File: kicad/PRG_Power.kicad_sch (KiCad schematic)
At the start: 18 parts, among them U1 4049

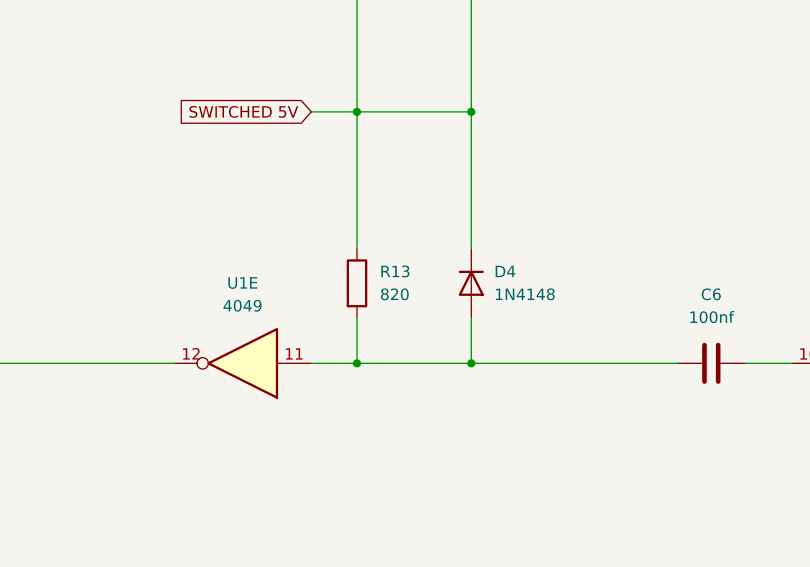
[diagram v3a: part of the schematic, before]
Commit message: Minor error - wrong resistor value as R13
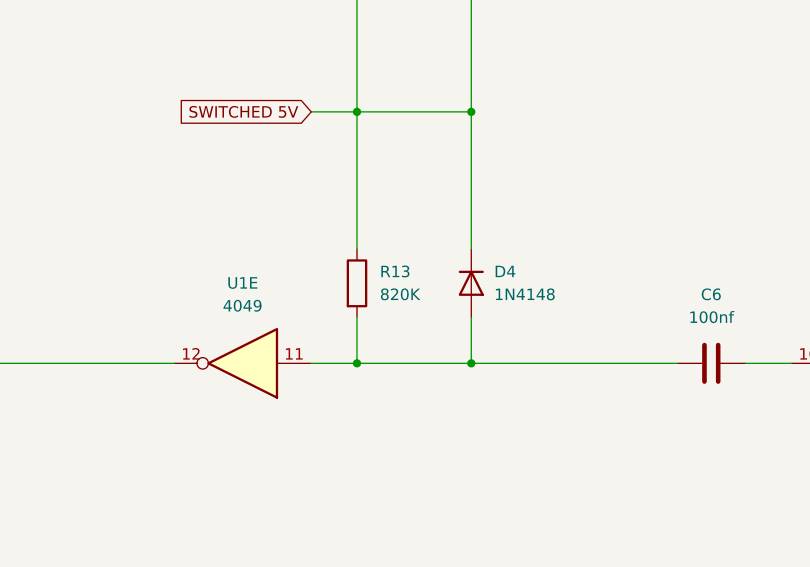
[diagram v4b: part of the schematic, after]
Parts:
- R13: value 820 -> 820K
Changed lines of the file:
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@@
   (title_block
     (title "EPROM Burner 2708 / 2716")
-    (date "2023-08-14")
-    (rev "2.5")
+    (date "2023-09-01")
+    (rev "2.6")
   )
   (junction (at 180.34 101.6) (diameter 0) (color 0 0 0 0)
@@
   (symbol (lib_id "Device:R") (at 180.34 92.71 0) (unit 1)
     (in_bom yes) (on_board yes) (dnp no) (fields_autoplaced)
-    (property "Reference" "R13" (at 182.88 91.4399 0)
-      (effects (font (size 1.27 1.27)) (justify left))
-    )
-    (property "Value" "820" (at 182.88 93.9799 0)
-      (effects (font (size 1.27 1.27)) (justify left))
-    )
+    (property "Reference" "R13" (at 182.88 91.44 0)
+      (effects (font (size 1.27 1.27)) (justify left))
+    )
+    (property "Value" "820K" (at 182.88 93.98 0)
+      (effects (font (size 1.27 1.27)) (justify left))
+    )

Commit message: Update docs
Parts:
- TR3, TR4, TR5: footprint Package_TO_SOT_THT:TO-92_Inline_Wide -> Package_TO_SOT_THT:TO-92_Inline
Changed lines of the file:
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@@
 (kicad_sch
-	(version 20231120)
+	(version 20250114)
 	(generator "eeschema")
-	(generator_version "8.0")
+	(generator_version "9.0")
 	(paper "A4")
 	(title_block
 		(title "EPROM Burner 2708 / 2716")
-		(date "2023-09-01")
-		(rev "2.6")
+		(date "2025-04-14")
+		(rev "2.7")
 	)
 	(junction
@@
 			)
 		)
-		(property "Footprint" "Package_TO_SOT_THT:TO-92_Inline_Wide"
+		(property "Footprint" "Package_TO_SOT_THT:TO-92_Inline"
 			(at 99.06 62.865 0)
 			(effects
@@
 			)
 		)
-		(property "Description" ""
+		(property "Description" "0.1A Ic, 30V Vce, PNP Small Signal Transistor, TO-92"
 			(at 104.14 60.96 0)
 			(effects
@@
 			)
 		)
-		(property "Description" ""
+		(property "Description" "Power symbol creates a global label with name \"GND\" , ground"
 			(at 116.84 38.1 0)
 			(effects
@@
 			)
 		)
-		(property "Description" ""
+		(property "Description" "Resistor"
 			(at 180.34 92.71 0)
 			(effects
@@
 			)
 		)
-		(property "Description" ""
+		(property "Description" "100V 0.15A standard switching diode, DO-35"
+			(at 193.04 92.71 0)
+			(effects
+				(font
+					(size 1.27 1.27)
+				)
+				(hide yes)
+			)
+		)
+		(property "Sim.Device" "D"
+			(at 193.04 92.71 0)
+			(effects
+				(font
+					(size 1.27 1.27)
+				)
+				(hide yes)
+			)
+		)
+		(property "Sim.Pins" "1=K 2=A"
 			(at 193.04 92.71 0)
 			(effects
@@
 			)
 		)
-		(property "Footprint" "Package_TO_SOT_THT:TO-92_Inline_Wide"
+		(property "Footprint" "Package_TO_SOT_THT:TO-92_Inline"
 			(at 121.92 46.355 0)
 			(effects
@@
 			)
 		)
-		(property "Description" ""
+		(property "Description" "0.1A Ic, 30V Vce, Small Signal NPN Transistor, TO-92"
 			(at 127 48.26 0)
 			(effects
@@
 			)
 		)
-		(property "Description" ""
+		(property "Description" "Unpolarized capacitor"
 			(at 219.71 101.6 0)
 			(effects
@@
 			)
 		)
-		(property "Description" ""
+		(property "Description" "Resistor"
 			(at 115.57 30.48 0)
 			(effects
@@
 			)
 		)
-		(property "Description" ""
+		(property "Description" "Power symbol creates a global label with name \"GND\" , ground"
 			(at 261.62 116.84 0)
 			(effects
@@
 			)
 		)
-		(property "Description" ""
+		(property "Description" "Power symbol creates a global label with name \"GND\" , ground"
 			(at 86.36 25.4 0)
 			(effects
@@
 			)
 		)
-		(property "Description" ""
+		(property "Description" "Resistor"
 			(at 109.22 69.85 0)
 			(effects
@@
 			)
 		)
-		(property "Description" ""
+		(property "Description" "Unpolarized capacitor"
 			(at 60.96 59.69 0)
 			(effects
@@
 			)
 		)
-		(property "Description" ""
+		(property "Description" "Resistor"
 			(at 101.6 41.91 0)
 			(effects
@@
 			)
 		)
-		(property "Description" ""
+		(property "Description" "Resistor"
 			(at 261.62 110.49 0)
 			(effects
@@
 			)
 		)
-		(property "Description" ""
+		(property "Description" "Hex Buffer Inverter"
 			(at 149.86 40.64 0)
 			(effects
@@
 			)
 		)
-		(property "Description" ""
+		(property "Description" "Resistor"
 			(at 115.57 60.96 0)
 			(effects
@@
 			)
 		)
-		(property "Description" ""
+		(property "Description" "Unpolarized capacitor"
 			(at 217.17 48.26 0)
 			(effects
@@
 			)
 		)
-		(property "Footprint" "Package_TO_SOT_THT:TO-92_Inline_Wide"
+		(property "Footprint" "Package_TO_SOT_THT:TO-92_Inline"
 			(at 99.06 28.575 0)
 			(effects
@@
 			)
 		)
-		(property "Description" ""
+		(property "Description" "0.1A Ic, 30V Vce, Small Signal NPN Transistor, TO-92"
 			(at 104.14 30.48 0)
 			(effects
@@
 			)
 		)
-		(property "Description" ""
+		(property "Description" "Hex Buffer Inverter"
 			(at 167.64 101.6 0)
 			(effects
@@
 			)
 		)
-		(property "Description" ""
+		(property "Description" "Resistor"
 			(at 140.97 48.26 0)
 			(effects
@@
 			)
 		)
-		(property "Description" ""
+		(property "Description" "Power symbol creates a global label with name \"GND\" , ground"
 			(at 60.96 63.5 0)
 			(effects
@@
 			)
 		)
-		(property "Description" ""
+		(property "Description" "Hex Buffer Inverter"
 			(at 236.22 101.6 0)
 			(effects
@@
 			)
 		)
-		(property "Description" ""
+		(property "Description" "Resistor"
 			(at 180.34 57.15 0)
 			(effects
@@
 			)
 		)
-		(property "Description" ""
+		(property "Description" "100V 0.15A standard switching diode, DO-35"
+			(at 193.04 57.15 0)
+			(effects
+				(font
+					(size 1.27 1.27)
+				)
+				(hide yes)
+			)
+		)
+		(property "Sim.Device" "D"
+			(at 193.04 57.15 0)
+			(effects
+				(font
+					(size 1.27 1.27)
+				)
+				(hide yes)
+			)
+		)
+		(property "Sim.Pins" "1=K 2=A"
 			(at 193.04 57.15 0)
 			(effects
@@
 			)
 		)
-		(property "Description" ""
+		(property "Description" "Hex Buffer Inverter"
 			(at 167.64 48.26 0)
 			(effects
@@
 			)
 		)
-		(property "Description" ""
+		(property "Description" "Resistor"
 			(at 80.01 50.8 0)
 			(effects
@@
 			)
 		)
-		(property "Description" ""
+		(property "Description" "Hex Buffer Inverter"
 			(at 233.68 48.26 0)
 			(effects

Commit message: Update footprints
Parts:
- D3, D4: footprint Diode_THT:D_DO-35_SOD27_P7.62mm_Horizontal -> Diode_THT:D_DO-41_SOD81_P10.16mm_Horizontal
- TR3, TR4, TR5: footprint Package_TO_SOT_THT:TO-92_Inline -> Package_TO_SOT_THT:TO-92_Inline_Wide
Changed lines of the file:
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@@
 			)
 		)
-		(property "Footprint" "Package_TO_SOT_THT:TO-92_Inline"
+		(property "Footprint" "Package_TO_SOT_THT:TO-92_Inline_Wide"
 			(at 99.06 62.865 0)
 			(effects
@@
 			)
 		)
-		(property "Footprint" "Diode_THT:D_DO-35_SOD27_P7.62mm_Horizontal"
+		(property "Footprint" "Diode_THT:D_DO-41_SOD81_P10.16mm_Horizontal"
 			(at 188.595 92.71 0)
 			(effects
@@
 			)
 		)
-		(property "Footprint" "Package_TO_SOT_THT:TO-92_Inline"
+		(property "Footprint" "Package_TO_SOT_THT:TO-92_Inline_Wide"
 			(at 121.92 46.355 0)
 			(effects
@@
 			)
 		)
-		(property "Footprint" "Package_TO_SOT_THT:TO-92_Inline"
+		(property "Footprint" "Package_TO_SOT_THT:TO-92_Inline_Wide"
 			(at 99.06 28.575 0)
 			(effects
@@
 			)
 		)
-		(property "Footprint" "Diode_THT:D_DO-35_SOD27_P7.62mm_Horizontal"
+		(property "Footprint" "Diode_THT:D_DO-41_SOD81_P10.16mm_Horizontal"
 			(at 197.485 57.15 0)
 			(effects
